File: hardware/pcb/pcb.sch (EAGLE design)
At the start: 18 parts, among them IC1 LM1117MPX-ADJ

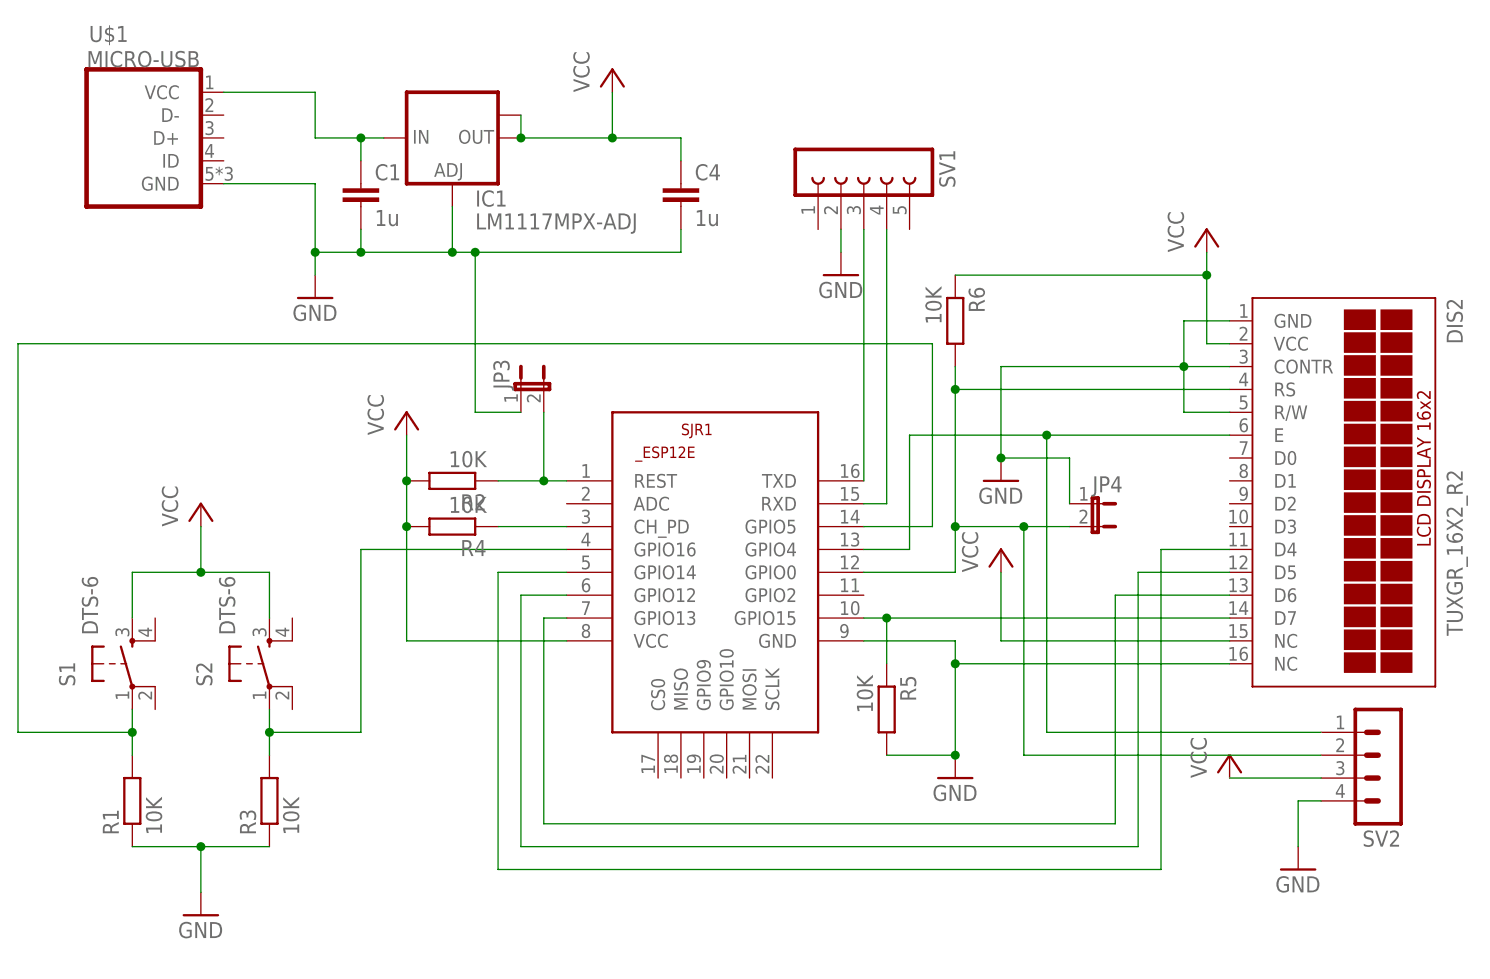
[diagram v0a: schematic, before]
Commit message: debugged pcb, which is now working
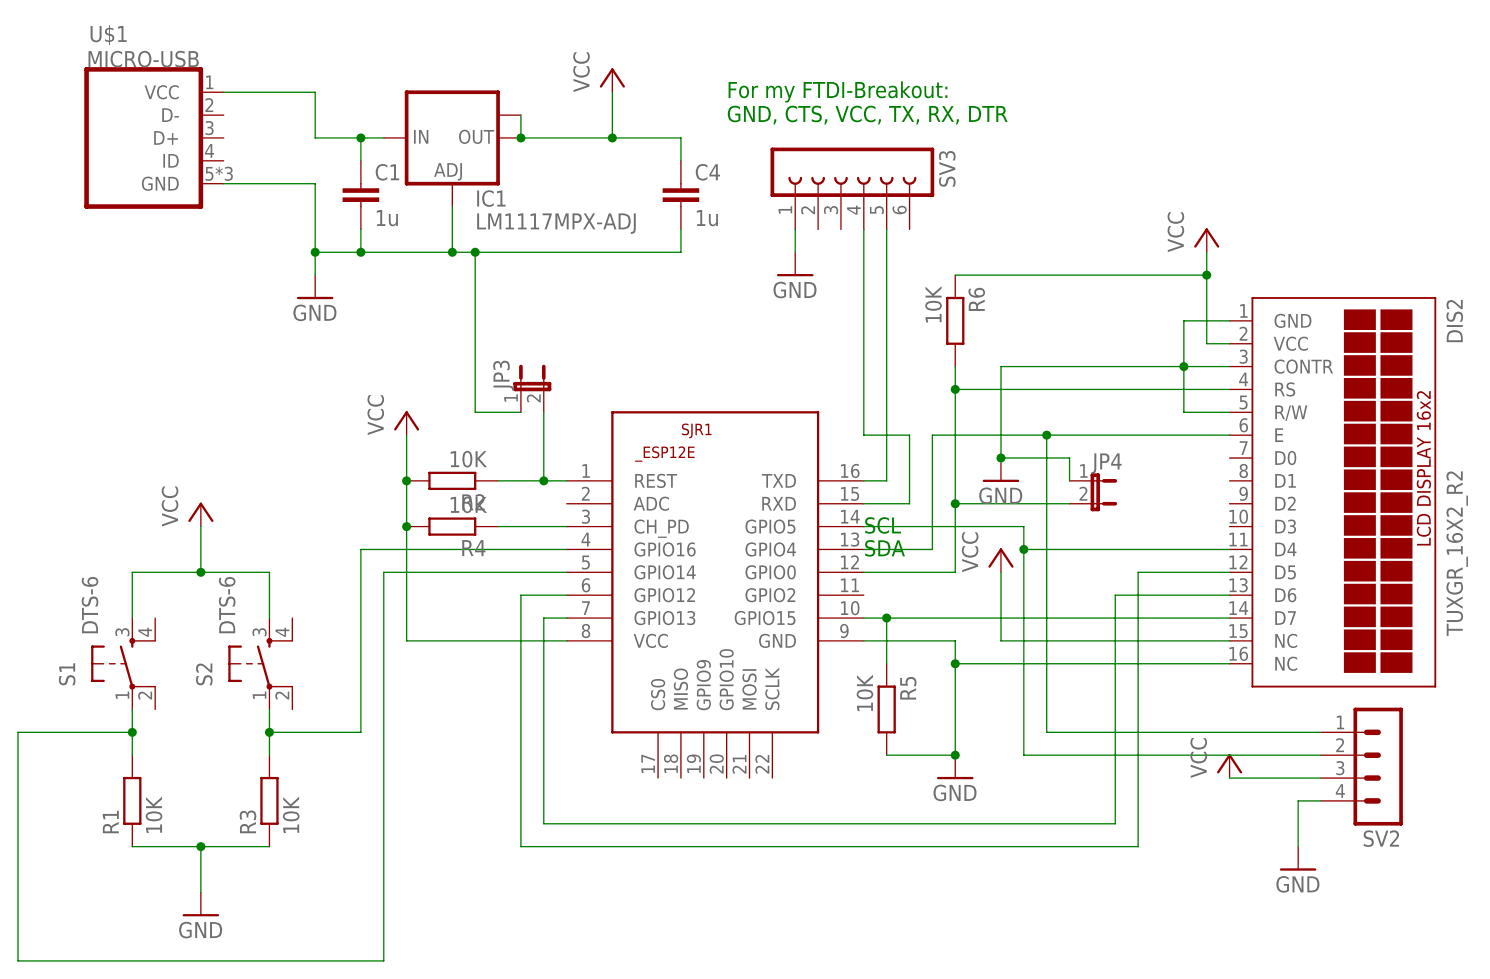
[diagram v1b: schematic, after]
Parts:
- removed SV1: (no value), con-lsta:FE05-1
- added SV3: (no value), con-lsta:FE06-1
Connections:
- net GND: now also SV3.1; no longer SV1.2
- net N$1: now also SJR1.GPIO5, SV2.2; no longer SJR1.GPIO14
- net N$10: now also SV3.5; no longer SV1.3
- net N$5: no longer SV2.2
- net N$7: now also SJR1.GPIO14; no longer SJR1.GPIO5
- net N$9: now also SV3.4; no longer SV1.4
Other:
- note added: "For my FTDI-Breakout: GND, CTS, VCC, TX, RX, DTR"
- note added: "SCL"
- note added: "SDA"
- moved on the sheet: JP4
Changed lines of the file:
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@@
 <part name="C4" library="rcl" library_urn="urn:adsk.eagle:library:334" deviceset="C-EU" device="C0805" package3d_urn="urn:adsk.eagle:package:23617/2" value="1u"/>
 <part name="C1" library="rcl" library_urn="urn:adsk.eagle:library:334" deviceset="C-EU" device="C0805" package3d_urn="urn:adsk.eagle:package:23617/2" value="1u"/>
-<part name="SV1" library="con-lsta" library_urn="urn:adsk.eagle:library:161" deviceset="FE05-1" device="" package3d_urn="urn:adsk.eagle:package:8190/1"/>
 <part name="GND5" library="supply1" library_urn="urn:adsk.eagle:library:371" deviceset="GND" device=""/>
 <part name="R2" library="rcl" library_urn="urn:adsk.eagle:library:334" deviceset="R-EU_" device="R0805" package3d_urn="urn:adsk.eagle:package:23553/2" value="10K"/>
@@
 <part name="GND6" library="supply1" library_urn="urn:adsk.eagle:library:371" deviceset="GND" device=""/>
 <part name="P+6" library="supply1" library_urn="urn:adsk.eagle:library:371" deviceset="VCC" device=""/>
+<part name="SV3" library="con-lsta" library_urn="urn:adsk.eagle:library:161" deviceset="FE06-1" device="" package3d_urn="urn:adsk.eagle:package:8191/1"/>
 </parts>
 <sheets>
 <sheet>
 <plain>
+<text x="99.06" y="47.498" size="1.778" layer="91">SDA</text>
+<text x="99.06" y="50.038" size="1.778" layer="91">SCL</text>
+<text x="83.82" y="95.758" size="1.778" layer="91">For my FTDI-Breakout:
+GND, CTS, VCC, TX, RX, DTR</text>
 </plain>
 <instances>
@@
 <attribute name="VALUE" x="44.704" y="84.201" size="1.778" layer="96"/>
 </instance>
-<instance part="SV1" gate="G$1" x="99.06" y="91.44" smashed="yes" rot="R270">
-<attribute name="VALUE" x="88.9" y="92.71" size="1.778" layer="96" rot="R270"/>
-<attribute name="NAME" x="107.442" y="92.71" size="1.778" layer="95" rot="R270"/>
-</instance>
-<instance part="GND5" gate="1" x="96.52" y="78.74" smashed="yes">
-<attribute name="VALUE" x="93.98" y="76.2" size="1.778" layer="96"/>
+<instance part="GND5" gate="1" x="91.44" y="78.74" smashed="yes">
+<attribute name="VALUE" x="88.9" y="76.2" size="1.778" layer="96"/>
 </instance>
 <instance part="R2" gate="G$1" x="53.34" y="55.88" smashed="yes" rot="R180">
@@
 <attribute name="VALUE" x="66.675" y="66.04" size="1.778" layer="96" rot="R90"/>
 </instance>
-<instance part="JP4" gate="A" x="124.46" y="53.34" smashed="yes" rot="R270">
-<attribute name="NAME" x="124.46" y="54.61" size="1.778" layer="95"/>
-<attribute name="VALUE" x="124.46" y="47.625" size="1.778" layer="96"/>
+<instance part="JP4" gate="A" x="124.46" y="55.88" smashed="yes" rot="R270">
+<attribute name="NAME" x="124.46" y="57.15" size="1.778" layer="95"/>
+<attribute name="VALUE" x="124.46" y="50.165" size="1.778" layer="96"/>
 </instance>
 <instance part="SV2" gate="1" x="157.48" y="22.86" smashed="yes" rot="R180">
@@
 <instance part="P+6" gate="VCC" x="139.7" y="25.4" smashed="yes">
 <attribute name="VALUE" x="137.16" y="22.86" size="1.778" layer="96" rot="R90"/>
+</instance>
+<instance part="SV3" gate="G$1" x="96.52" y="91.44" smashed="yes" rot="R270">
+<attribute name="VALUE" x="86.36" y="92.71" size="1.778" layer="96" rot="R270"/>
+<attribute name="NAME" x="107.442" y="92.71" size="1.778" layer="95" rot="R270"/>
 </instance>
 </instances>
@@
 <net name="N$1" class="0">
 <segment>
-<pinref part="SJR1" gate="G$1" pin="GPIO14"/>
-<wire x1="66.04" y1="45.72" x2="58.42" y2="45.72" width="0.1524" layer="91"/>
-<wire x1="58.42" y1="45.72" x2="58.42" y2="12.7" width="0.1524" layer="91"/>
-<wire x1="58.42" y1="12.7" x2="132.08" y2="12.7" width="0.1524" layer="91"/>
-<wire x1="132.08" y1="12.7" x2="132.08" y2="48.26" width="0.1524" layer="91"/>
 <pinref part="DIS2" gate="G$1" pin="D4"/>
-<wire x1="132.08" y1="48.26" x2="139.7" y2="48.26" width="0.1524" layer="91"/>
+<pinref part="SV2" gate="1" pin="2"/>
+<wire x1="116.84" y1="25.4" x2="149.86" y2="25.4" width="0.1524" layer="91"/>
+<wire x1="116.84" y1="25.4" x2="116.84" y2="48.26" width="0.1524" layer="91"/>
+<wire x1="116.84" y1="48.26" x2="116.84" y2="50.8" width="0.1524" layer="91"/>
+<wire x1="116.84" y1="50.8" x2="99.06" y2="50.8" width="0.1524" layer="91"/>
+<pinref part="SJR1" gate="G$1" pin="GPIO5"/>
+<wire x1="139.7" y1="48.26" x2="116.84" y2="48.26" width="0.1524" layer="91"/>
+<junction x="116.84" y="48.26"/>
 </segment>
 </net>
@@
 <junction x="114.3" y="58.42"/>
 <pinref part="JP4" gate="A" pin="1"/>
-<wire x1="121.92" y1="58.42" x2="121.92" y2="53.34" width="0.1524" layer="91"/>
+<wire x1="121.92" y1="58.42" x2="121.92" y2="55.88" width="0.1524" layer="91"/>
 </segment>
 <segment>
@@
 <segment>
 <pinref part="GND5" gate="1" pin="GND"/>
-<pinref part="SV1" gate="G$1" pin="2"/>
-<wire x1="96.52" y1="81.28" x2="96.52" y2="83.82" width="0.1524" layer="91"/>
+<wire x1="91.44" y1="81.28" x2="91.44" y2="83.82" width="0.1524" layer="91"/>
+<pinref part="SV3" gate="G$1" pin="1"/>
 </segment>
 <segment>
@@
 <wire x1="17.78" y1="27.94" x2="5.08" y2="27.94" width="0.1524" layer="91"/>
 <junction x="17.78" y="27.94"/>
-<wire x1="5.08" y1="27.94" x2="5.08" y2="71.12" width="0.1524" layer="91"/>
-<wire x1="5.08" y1="71.12" x2="106.68" y2="71.12" width="0.1524" layer="91"/>
-<wire x1="106.68" y1="71.12" x2="106.68" y2="50.8" width="0.1524" layer="91"/>
-<pinref part="SJR1" gate="G$1" pin="GPIO5"/>
-<wire x1="106.68" y1="50.8" x2="99.06" y2="50.8" width="0.1524" layer="91"/>
+<pinref part="SJR1" gate="G$1" pin="GPIO14"/>
+<wire x1="66.04" y1="45.72" x2="45.72" y2="45.72" width="0.1524" layer="91"/>
+<wire x1="45.72" y1="45.72" x2="45.72" y2="2.54" width="0.1524" layer="91"/>
+<wire x1="45.72" y1="2.54" x2="5.08" y2="2.54" width="0.1524" layer="91"/>
+<wire x1="5.08" y1="2.54" x2="5.08" y2="27.94" width="0.1524" layer="91"/>
 </segment>
 </net>
@@
 <pinref part="SJR1" gate="G$1" pin="GPIO0"/>
 <wire x1="109.22" y1="68.58" x2="109.22" y2="66.04" width="0.1524" layer="91"/>
-<wire x1="109.22" y1="66.04" x2="109.22" y2="50.8" width="0.1524" layer="91"/>
-<wire x1="109.22" y1="50.8" x2="109.22" y2="45.72" width="0.1524" layer="91"/>
+<wire x1="109.22" y1="66.04" x2="109.22" y2="53.34" width="0.1524" layer="91"/>
+<wire x1="109.22" y1="53.34" x2="109.22" y2="45.72" width="0.1524" layer="91"/>
 <wire x1="109.22" y1="45.72" x2="99.06" y2="45.72" width="0.1524" layer="91"/>
 <pinref part="R6" gate="G$1" pin="2"/>
@@
 <junction x="109.22" y="66.04"/>
 <pinref part="JP4" gate="A" pin="2"/>
-<wire x1="121.92" y1="50.8" x2="116.84" y2="50.8" width="0.1524" layer="91"/>
-<junction x="109.22" y="50.8"/>
-<pinref part="SV2" gate="1" pin="2"/>
-<wire x1="116.84" y1="50.8" x2="109.22" y2="50.8" width="0.1524" layer="91"/>
-<junction x="116.84" y="50.8"/>
-<wire x1="116.84" y1="50.8" x2="116.84" y2="25.4" width="0.1524" layer="91"/>
-<wire x1="116.84" y1="25.4" x2="149.86" y2="25.4" width="0.1524" layer="91"/>
+<junction x="109.22" y="53.34"/>
+<wire x1="121.92" y1="53.34" x2="109.22" y2="53.34" width="0.1524" layer="91"/>
 </segment>
 </net>
@@
 <pinref part="DIS2" gate="G$1" pin="E"/>
 <pinref part="SJR1" gate="G$1" pin="GPIO4"/>
-<wire x1="104.14" y1="60.96" x2="104.14" y2="48.26" width="0.1524" layer="91"/>
-<wire x1="104.14" y1="48.26" x2="99.06" y2="48.26" width="0.1524" layer="91"/>
+<wire x1="106.68" y1="60.96" x2="106.68" y2="48.26" width="0.1524" layer="91"/>
+<wire x1="106.68" y1="48.26" x2="99.06" y2="48.26" width="0.1524" layer="91"/>
 <wire x1="139.7" y1="60.96" x2="119.38" y2="60.96" width="0.1524" layer="91"/>
 <pinref part="SV2" gate="1" pin="1"/>
-<wire x1="119.38" y1="60.96" x2="104.14" y2="60.96" width="0.1524" layer="91"/>
+<wire x1="119.38" y1="60.96" x2="106.68" y2="60.96" width="0.1524" layer="91"/>
 <junction x="119.38" y="60.96"/>
 <wire x1="119.38" y1="60.96" x2="119.38" y2="27.94" width="0.1524" layer="91"/>
@@
 </segment>
 </net>
-<net name="N$9" class="0">
-<segment>
-<pinref part="SJR1" gate="G$1" pin="RXD"/>
-<wire x1="99.06" y1="53.34" x2="101.6" y2="53.34" width="0.1524" layer="91"/>
-<wire x1="101.6" y1="53.34" x2="101.6" y2="83.82" width="0.1524" layer="91"/>
-<pinref part="SV1" gate="G$1" pin="4"/>
-</segment>
-</net>
-<net name="N$10" class="0">
-<segment>
-<pinref part="SJR1" gate="G$1" pin="TXD"/>
-<wire x1="99.06" y1="83.82" x2="99.06" y2="55.88" width="0.1524" layer="91"/>
-<pinref part="SV1" gate="G$1" pin="3"/>
-</segment>
-</net>
 <net name="N$12" class="0">
 <segment>
@@
 </segment>
 </net>
+<net name="N$9" class="0">
+<segment>
+<pinref part="SV3" gate="G$1" pin="4"/>
+<wire x1="99.06" y1="83.82" x2="99.06" y2="60.96" width="0.1524" layer="91"/>
+<pinref part="SJR1" gate="G$1" pin="RXD"/>
+<wire x1="99.06" y1="53.34" x2="104.14" y2="53.34" width="0.1524" layer="91"/>
+<wire x1="104.14" y1="53.34" x2="104.14" y2="60.96" width="0.1524" layer="91"/>
+<wire x1="104.14" y1="60.96" x2="99.06" y2="60.96" width="0.1524" layer="91"/>
+</segment>
+</net>
+<net name="N$10" class="0">
+<segment>
+<pinref part="SV3" gate="G$1" pin="5"/>
+<wire x1="101.6" y1="83.82" x2="101.6" y2="55.88" width="0.1524" layer="91"/>
+<pinref part="SJR1" gate="G$1" pin="TXD"/>
+<wire x1="101.6" y1="55.88" x2="99.06" y2="55.88" width="0.1524" layer="91"/>
+</segment>
+</net>
 </nets>
 </sheet>
@@
 </drawing>
 <compatibility>
+<note version="6.3" minversion="6.2.2" severity="warning">
+Since Version 6.2.2 text objects can contain more than one line,
+which will not be processed correctly with this version.
+</note>
 <note version="8.2" severity="warning">
 Since Version 8.2, EAGLE supports online libraries. The ids
